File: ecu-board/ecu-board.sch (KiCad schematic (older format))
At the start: 0 parts

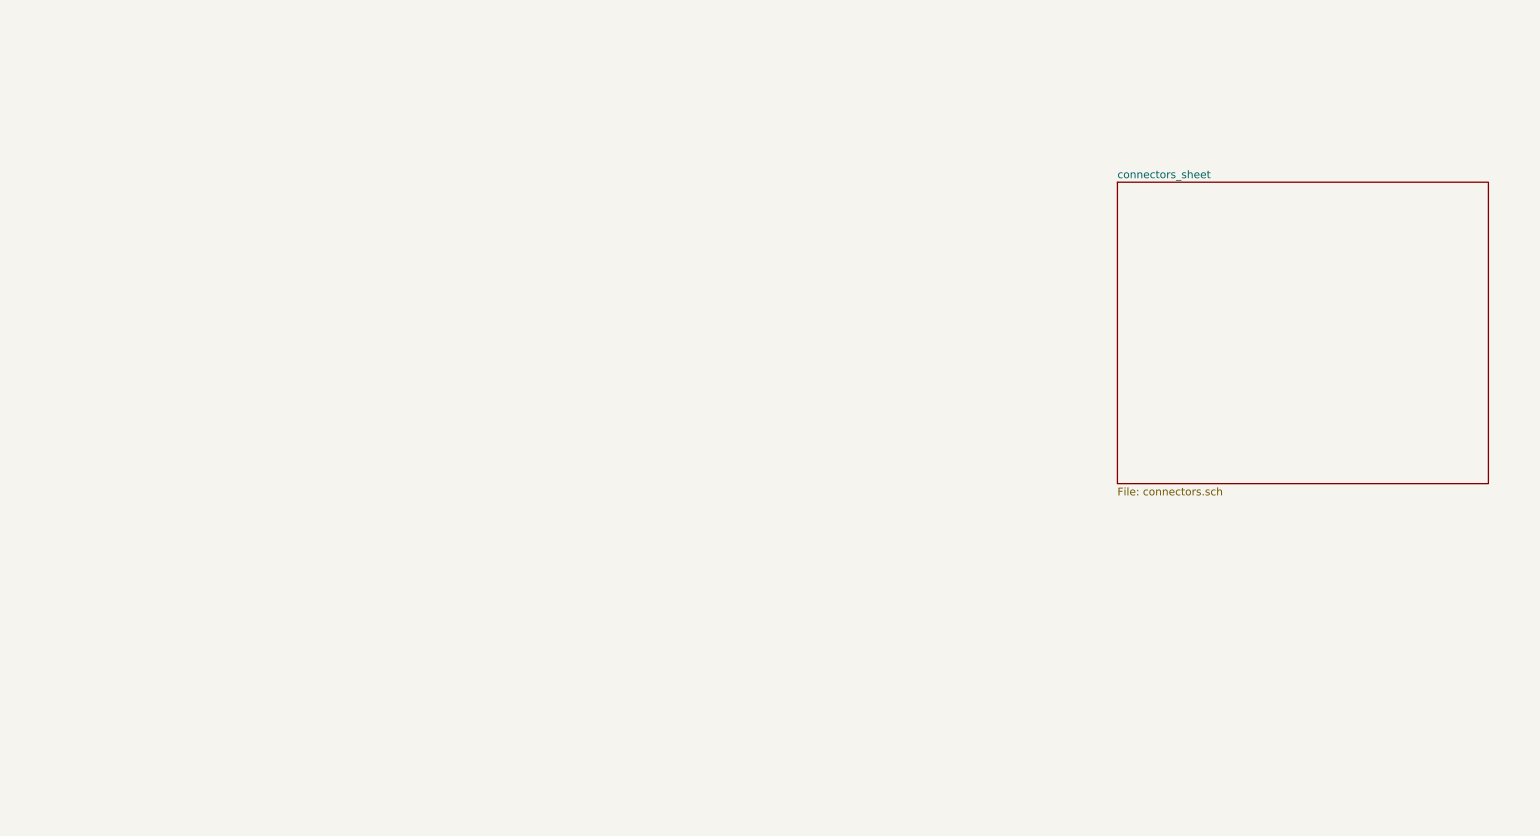
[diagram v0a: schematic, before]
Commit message: Schematic completed. Now to confirm details and proof-read.
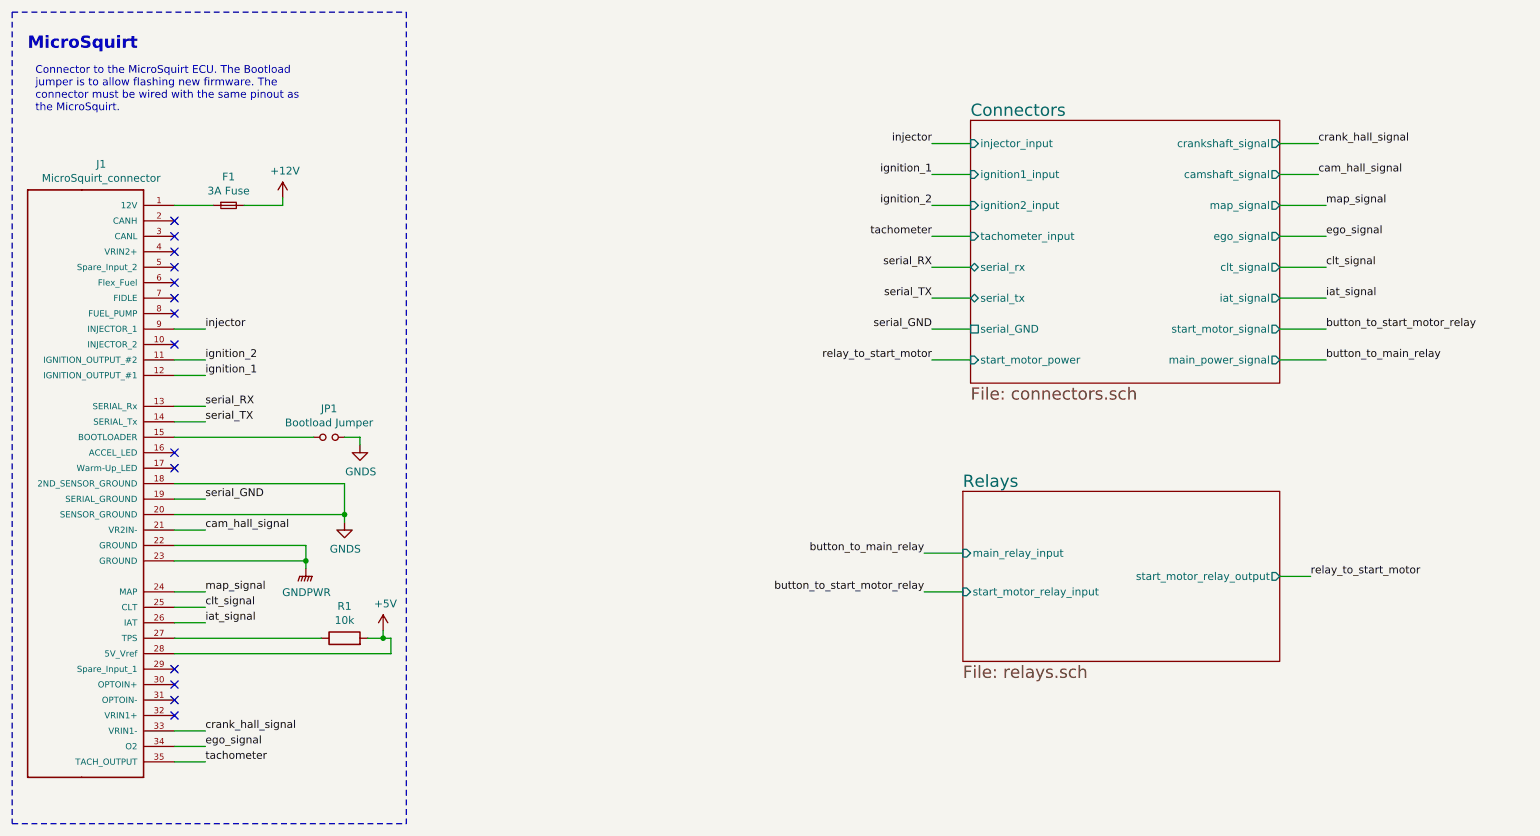
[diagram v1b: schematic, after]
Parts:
- added F1: 3A Fuse, symbol Device:Fuse_Small
- added J1: MicroSquirt_connector, TE_1-776230-1, symbol ecu-board:MicroSquirt_Connector
- added JP1: Bootload Jumper, symbol Device:Jumper_NO_Small
- added R1: 10k, symbol Device:R
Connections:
- new net: F1.1, J1.1 (12V)
- new net: J1.15 (BOOTLOADER), JP1.1
- new net: J1.27 (TPS), R1.1
- new net +12V: F1.2
- new net +5V: J1.28 (5V_Vref), R1.2
- new net GNDPWR: J1.22 (GROUND), J1.23 (GROUND)
- new net GNDS: J1.18 (2ND_SENSOR_GROUND), J1.20 (SENSOR_GROUND), JP1.2
- new net cam_hall_signal: J1.21 (VR2IN-)
- new net clt_signal: J1.25 (CLT)
- new net crank_hall_signal: J1.33 (VRIN1-)
- new net ego_signal: J1.34 (O2)
- new net iat_signal: J1.26 (IAT)
- new net ignition_1: J1.12 (IGNITION_OUTPUT_#1)
- new net ignition_2: J1.11 (IGNITION_OUTPUT_#2)
- new net injector: J1.9 (INJECTOR_1)
- new net map_signal: J1.24 (MAP)
- new net serial_GND: J1.19 (SERIAL_GROUND)
- new net serial_RX: J1.13 (SERIAL_Rx)
- new net serial_TX: J1.14 (SERIAL_Tx)
- new net tachometer: J1.35 (TACH_OUTPUT)
- no-connect marks 0 -> 14
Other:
- note added: "Connector to the MicroSquirt ECU. The Bootload \njumper is to allow flashing new firmware. The \nconnector must be wired with the same pinout as\nthe MicroSquirt."
- note added: "MicroSquirt"

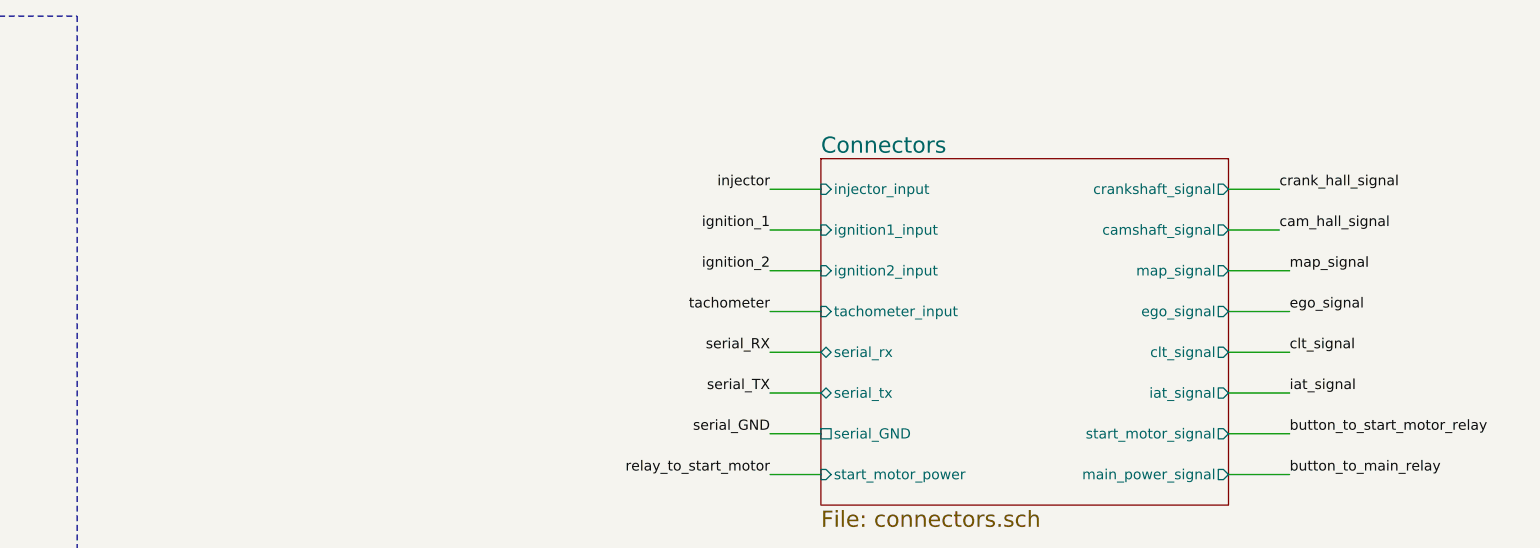
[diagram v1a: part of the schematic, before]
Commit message: Mount MAP sensor to PCB. Reverse injector input.
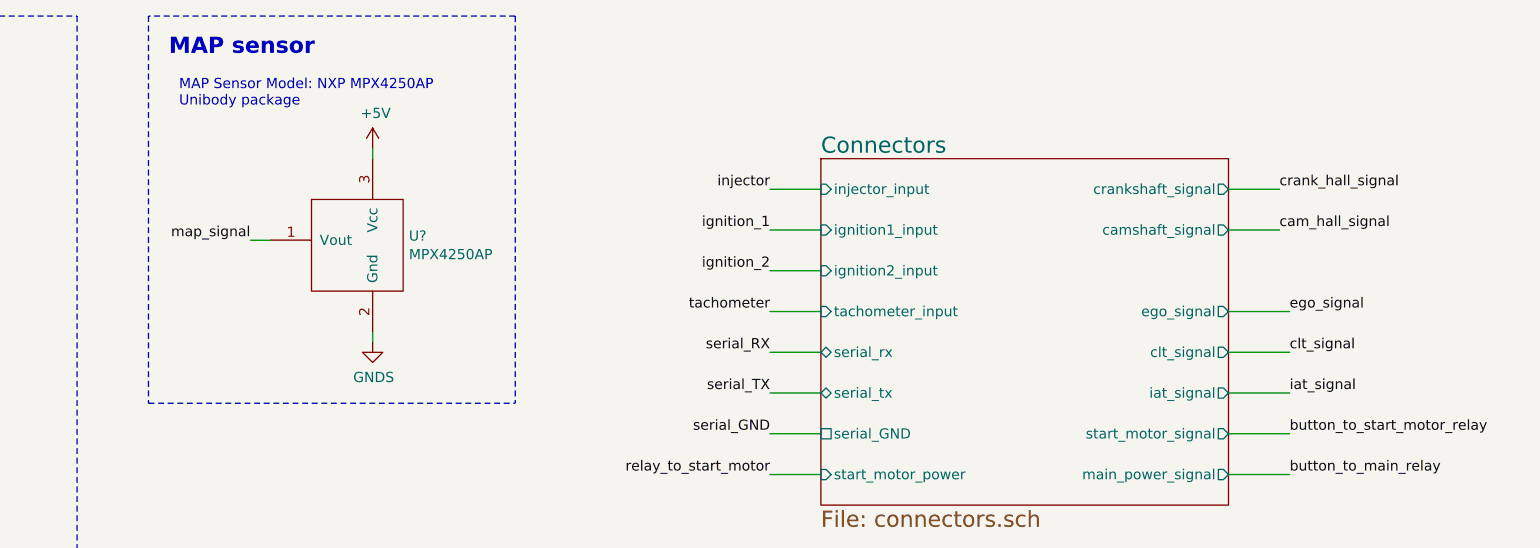
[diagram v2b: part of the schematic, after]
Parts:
- added U?: MPX4250AP, symbol ecu-board:MPX4250AP
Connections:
- net +5V: now also U?.3 (Vcc)
- net GNDS: now also U?.2 (Gnd)
- net map_signal: now also U?.1 (Vout)
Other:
- note added: "MAP Sensor Model: NXP MPX4250AP\nUnibody package"
- note added: "MAP sensor"
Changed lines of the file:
@@
 F2 "crankshaft_signal" O R 9400 1900 50
 F3 "camshaft_signal" O R 9400 2100 50
-F4 "map_signal" O R 9400 2300 50
-F5 "ego_signal" O R 9400 2500 50
-F6 "serial_rx" B L 7400 2700 50
-F7 "serial_tx" B L 7400 2900 50
-F8 "injector_input" I L 7400 1900 50
-F9 "clt_signal" O R 9400 2700 50
-F10 "iat_signal" O R 9400 2900 50
-F11 "start_motor_signal" O R 9400 3100 50
-F12 "main_power_signal" O R 9400 3300 50
-F13 "start_motor_power" I L 7400 3300 50
-F14 "ignition1_input" I L 7400 2100 50
-F15 "ignition2_input" I L 7400 2300 50
-F16 "serial_GND" U L 7400 3100 50
-F17 "tachometer_input" I L 7400 2500 50
+F4 "ego_signal" O R 9400 2500 50
+F5 "serial_rx" B L 7400 2700 50
+F6 "serial_tx" B L 7400 2900 50
+F7 "injector_input" I L 7400 1900 50
+F8 "clt_signal" O R 9400 2700 50
+F9 "iat_signal" O R 9400 2900 50
+F10 "start_motor_signal" O R 9400 3100 50
+F11 "main_power_signal" O R 9400 3300 50
+F12 "start_motor_power" I L 7400 3300 50
+F13 "ignition1_input" I L 7400 2100 50
+F14 "ignition2_input" I L 7400 2300 50
+F15 "serial_GND" U L 7400 3100 50
+F16 "tachometer_input" I L 7400 2500 50
 $EndSheet
 $Comp
@@
 NoConn ~ 2250 3900
 NoConn ~ 2250 4000
-Text Label 9700 2300 0    50   ~ 0
+Text Label 4600 2150 2    50   ~ 0
 map_signal
 Wire Wire Line
@@
 Wire Wire Line
 	9400 2500 9700 2500
-Wire Wire Line
-	9700 2300 9400 2300
 Text Label 2450 5800 0    50   ~ 0
 ego_signal
+Text Notes 4200 1250 0    79   ~ 16
+MAP sensor
+$Comp
+L power:+5V #PWR?
+U 1 1 5C731B42
+P 5200 1700
+AR Path="/5C5705F6/5C731B42" Ref="#PWR?"  Part="1"
+AR Path="/5C731B42" Ref="#PWR?"  Part="1"
+F 0 "#PWR?" H 5200 1550 50  0001 C CNN
+F 1 "+5V" H 5215 1873 50  0000 C CNN
+F 2 "" H 5200 1700 50  0001 C CNN
+F 3 "" H 5200 1700 50  0001 C CNN
+	1    5200 1700
+	1    0    0    -1
+$EndComp
+$Comp
+L power:GNDS #PWR?
+U 1 1 5C731B4A
+P 5200 2650
+AR Path="/5C5705F6/5C731B4A" Ref="#PWR?"  Part="1"
+AR Path="/5C731B4A" Ref="#PWR?"  Part="1"
+F 0 "#PWR?" H 5200 2400 50  0001 C CNN
+F 1 "GNDS" H 5205 2477 50  0000 C CNN
+F 2 "" H 5200 2650 50  0001 C CNN
+F 3 "" H 5200 2650 50  0001 C CNN
+	1    5200 2650
+	1    0    0    -1
+$EndComp
+Text Notes 4250 1500 0    50   ~ 0
+MAP Sensor Model: NXP MPX4250AP\nUnibody package
+Wire Notes Line
+	5900 1050 4100 1050
+$Comp
+L ecu-board:MPX4250AP U?
+U 1 1 5C731B59
+P 5200 2150
+AR Path="/5C5705F6/5C731B59" Ref="U?"  Part="1"
+AR Path="/5C731B59" Ref="U?"  Part="1"
+F 0 "U?" H 5022 2171 50  0000 R CNN
+F 1 "MPX4250AP" H 5022 2080 50  0000 R CNN
+F 2 "" H 5200 2050 50  0001 C CNN
+F 3 "" H 5200 2050 50  0001 C CNN
+	1    5200 2150
+	-1   0    0    -1
+$EndComp
+Wire Wire Line
+	5200 1700 5200 1750
+Wire Wire Line
+	5200 2600 5200 2650
+Wire Wire Line
+	4600 2150 4700 2150
+Wire Notes Line
+	4100 2950 5900 2950
+Wire Notes Line
+	5900 1050 5900 2950
+Wire Notes Line
+	4100 1050 4100 2950
 $EndSCHEMATC

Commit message: Cockpit connector expanded and merged with button connector. Injector connected to dead man's switch.
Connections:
- net serial_GND is gone; now on net GNDS: J1.19 (SERIAL_GROUND)
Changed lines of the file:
@@
 F13 "ignition1_input" I L 7400 2100 50
 F14 "ignition2_input" I L 7400 2300 50
-F15 "serial_GND" U L 7400 3100 50
-F16 "tachometer_input" I L 7400 2500 50
+F15 "tachometer_input" I L 7400 2500 50
 $EndSheet
 $Comp
@@
 L power:GNDS #PWR03
 U 1 1 5C63E8F3
-P 3350 4350
-F 0 "#PWR03" H 3350 4100 50  0001 C CNN
-F 1 "GNDS" H 3355 4177 50  0000 C CNN
-F 2 "" H 3350 4350 50  0001 C CNN
-F 3 "" H 3350 4350 50  0001 C CNN
-	1    3350 4350
+P 2600 4100
+F 0 "#PWR03" H 2600 3850 50  0001 C CNN
+F 1 "GNDS" H 2605 3927 50  0000 C CNN
+F 2 "" H 2600 4100 50  0001 C CNN
+F 3 "" H 2600 4100 50  0001 C CNN
+	1    2600 4100
 	1    0    0    -1
 $EndComp
@@
 Wire Wire Line
 	2450 4400 2250 4400
-Wire Wire Line
-	3350 4300 3350 4350
-Wire Wire Line
-	2250 4300 3350 4300
-Wire Wire Line
-	2250 4100 3350 4100
-Wire Wire Line
-	3350 4100 3350 4300
-Connection ~ 3350 4300
-Wire Wire Line
-	2250 4200 2450 4200
-Text Label 7150 3100 2    50   ~ 0
-serial_GND
-Wire Wire Line
-	7150 3100 7400 3100
-Text Label 2450 4200 0    50   ~ 0
-serial_GND
 Text Label 7150 2700 2    50   ~ 0
 serial_RX
@@
 Wire Notes Line
 	4100 1050 4100 2950
+Wire Wire Line
+	2250 4100 2350 4100
+Wire Wire Line
+	2250 4200 2350 4200
+Wire Wire Line
+	2350 4200 2350 4100
+Connection ~ 2350 4100
+Wire Wire Line
+	2350 4100 2600 4100
+Wire Wire Line
+	2250 4300 2350 4300
+Wire Wire Line
+	2350 4300 2350 4200
+Connection ~ 2350 4200
 $EndSCHEMATC

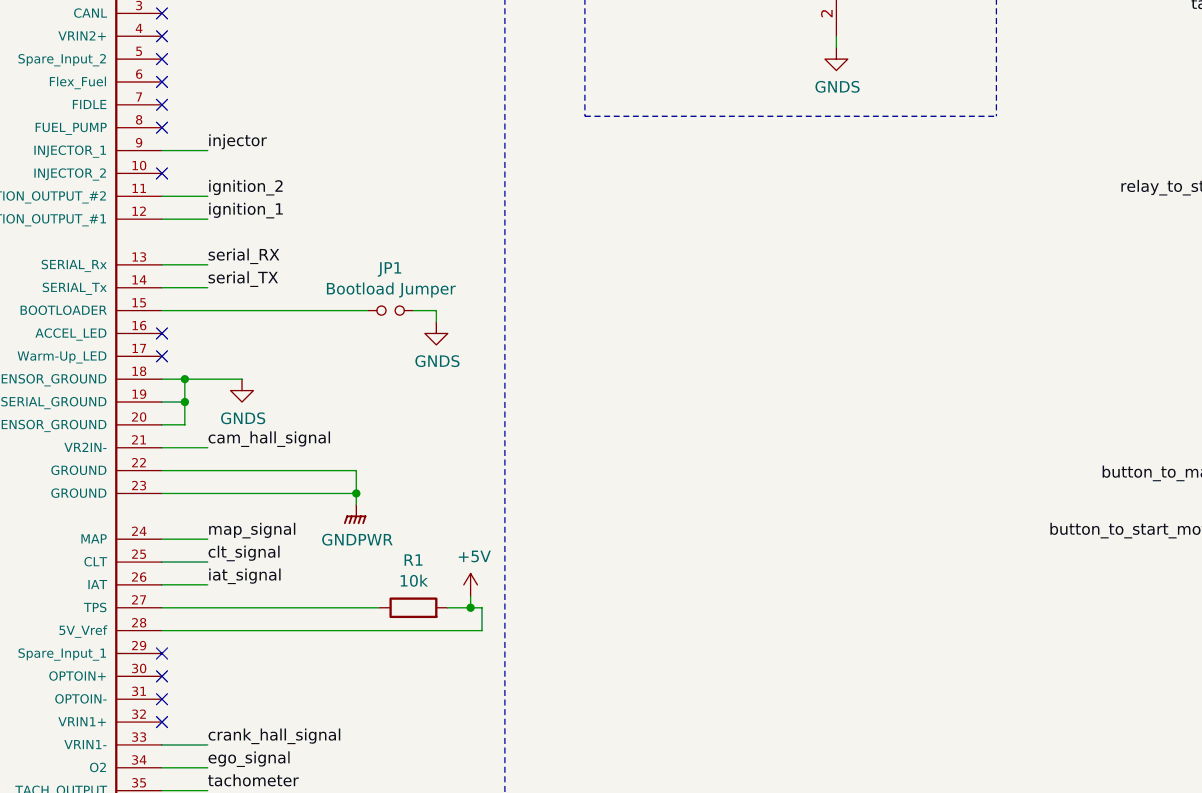
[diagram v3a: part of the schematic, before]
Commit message: Change TPS. Resolved #27.
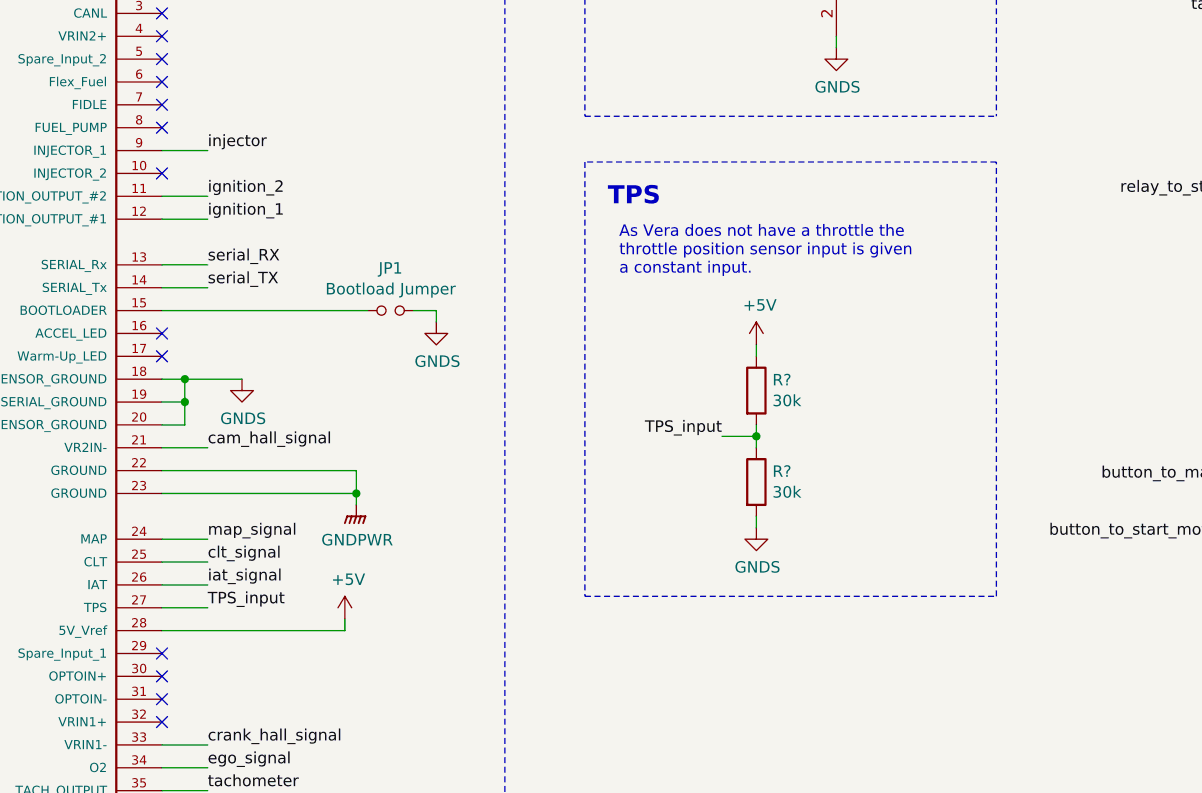
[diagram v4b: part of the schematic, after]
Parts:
- removed R1: 10k, symbol Device:R
- added R? (x2): 30k, symbol Device:R
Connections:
- net +5V: now also R?.1
- net GNDS: now also R?.2
- net TPS_input: now reaches J1.27 (TPS)
- net TPS_input: now also R?.1, R?.2
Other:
- note added: "As Vera does not have a throttle the \nthrottle position sensor input is given \na constant input."
- note added: "TPS"
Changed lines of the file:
@@
 Text Label 7150 2300 2    50   ~ 0
 ignition_2
-$Comp
-L Device:R R1
-U 1 1 5C68220A
-P 3350 5100
-F 0 "R1" V 3557 5100 50  0000 C CNN
-F 1 "10k" V 3466 5100 50  0000 C CNN
-F 2 "" V 3280 5100 50  0001 C CNN
-F 3 "~" H 3350 5100 50  0001 C CNN
-F 4 "1700251" H 750 250 50  0001 C CNN "Farnell"
-	1    3350 5100
-	0    -1   -1   0
-$EndComp
 Wire Wire Line
-	3500 5100 3600 5100
-Wire Wire Line
-	2250 5100 3200 5100
-Wire Wire Line
-	2250 5200 3650 5200
+	2250 5200 3050 5200
 NoConn ~ 2250 3000
 NoConn ~ 2250 2900
@@
 L power:+5V #PWR05
 U 1 1 5C692295
-P 3600 5050
-F 0 "#PWR05" H 3600 4900 50  0001 C CNN
-F 1 "+5V" H 3615 5223 50  0000 C CNN
-F 2 "" H 3600 5050 50  0001 C CNN
-F 3 "" H 3600 5050 50  0001 C CNN
-	1    3600 5050
+P 3050 5150
+F 0 "#PWR05" H 3050 5000 50  0001 C CNN
+F 1 "+5V" H 3065 5323 50  0000 C CNN
+F 2 "" H 3050 5150 50  0001 C CNN
+F 3 "" H 3050 5150 50  0001 C CNN
+	1    3050 5150
 	1    0    0    -1
 $EndComp
-Wire Wire Line
-	3650 5100 3650 5200
-Wire Wire Line
-	3600 5100 3600 5050
-Connection ~ 3600 5100
-Wire Wire Line
-	3600 5100 3650 5100
 Wire Wire Line
 	9650 1900 9400 1900
@@
 	2350 4300 2350 4200
 Connection ~ 2350 4200
+Text Notes 4200 3350 0    79   ~ 16
+TPS
+Text Notes 4250 3650 0    50   ~ 0
+As Vera does not have a throttle the \nthrottle position sensor input is given \na constant input.
+Text Label 2450 5100 0    50   ~ 0
+TPS_input
+Wire Wire Line
+	2450 5100 2250 5100
+Wire Wire Line
+	3050 5150 3050 5200
+Text Label 4700 4350 2    50   ~ 0
+TPS_input
+$Comp
+L Device:R R?
+U 1 1 5C9A98F2
+P 4850 4150
+F 0 "R?" H 4920 4196 50  0000 L CNN
+F 1 "30k" H 4920 4105 50  0000 L CNN
+F 2 "" V 4780 4150 50  0001 C CNN
+F 3 "~" H 4850 4150 50  0001 C CNN
+	1    4850 4150
+	1    0    0    -1
+$EndComp
+$Comp
+L Device:R R?
+U 1 1 5C9A9924
+P 4850 4550
+F 0 "R?" H 4920 4596 50  0000 L CNN
+F 1 "30k" H 4920 4505 50  0000 L CNN
+F 2 "" V 4780 4550 50  0001 C CNN
+F 3 "~" H 4850 4550 50  0001 C CNN
+	1    4850 4550
+	1    0    0    -1
+$EndComp
+Wire Wire Line
+	4850 4300 4850 4350
+Wire Wire Line
+	4850 4350 4700 4350
+Connection ~ 4850 4350
+Wire Wire Line
+	4850 4350 4850 4400
+Wire Wire Line
+	4850 3950 4850 4000
+$Comp
+L power:GNDS #PWR?
+U 1 1 5C9ADA95
+P 4850 4750
+F 0 "#PWR?" H 4850 4500 50  0001 C CNN
+F 1 "GNDS" H 4855 4577 50  0000 C CNN
+F 2 "" H 4850 4750 50  0001 C CNN
+F 3 "" H 4850 4750 50  0001 C CNN
+	1    4850 4750
+	1    0    0    -1
+$EndComp
+Wire Wire Line
+	4850 4750 4850 4700
+Wire Notes Line
+	4100 3150 4100 5050
+Wire Notes Line
+	4100 5050 5900 5050
+Wire Notes Line
+	5900 5050 5900 3150
+Wire Notes Line
+	5900 3150 4100 3150
+$Comp
+L power:+5V #PWR?
+U 1 1 5C9B7680
+P 4850 3950
+F 0 "#PWR?" H 4850 3800 50  0001 C CNN
+F 1 "+5V" H 4865 4123 50  0000 C CNN
+F 2 "" H 4850 3950 50  0001 C CNN
+F 3 "" H 4850 3950 50  0001 C CNN
+	1    4850 3950
+	1    0    0    -1
+$EndComp
 $EndSCHEMATC
